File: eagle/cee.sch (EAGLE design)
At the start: 46 parts, among them IC1 IC1, J1 SOLDERJUMPERNC2

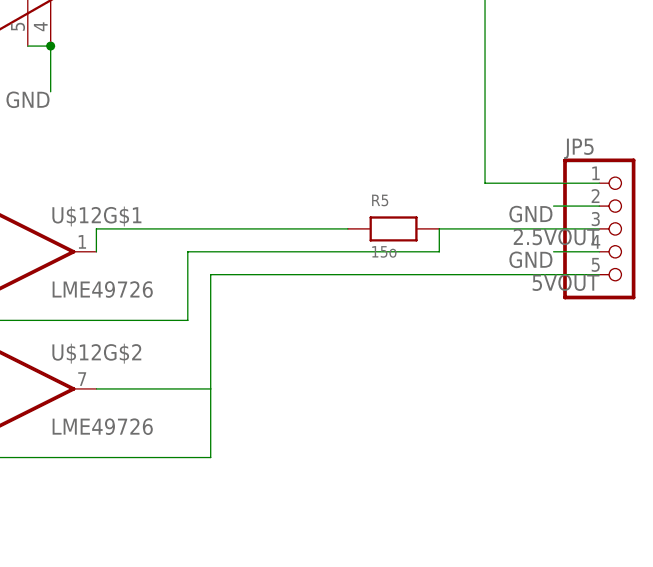
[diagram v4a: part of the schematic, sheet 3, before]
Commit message: pulldown resistor, chanB as input, moved capacitors, updated sc70, cleaned routing
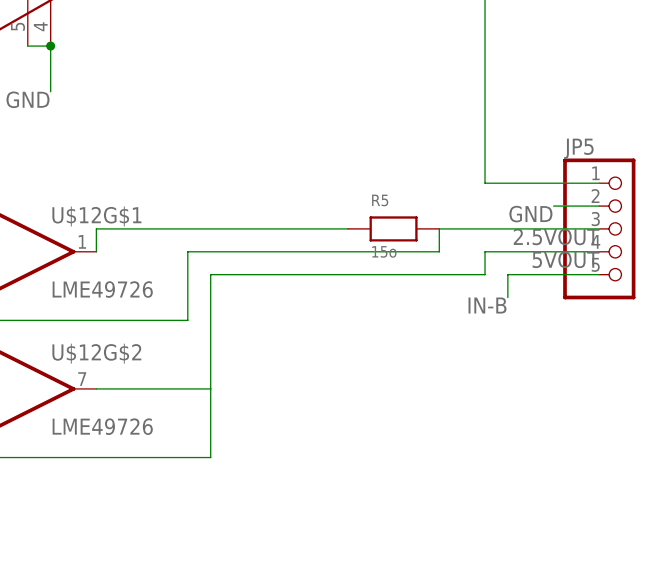
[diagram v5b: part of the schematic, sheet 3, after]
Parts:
- added R7: (no value), nonolith:RESISTOR0603
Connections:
- new net IN-B: JP5.5, R7.2, RN2C.1
- net 5VOUT: now also JP5.4; no longer JP5.5
- net GND: now also R7.1; no longer JP5.4
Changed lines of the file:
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@@
 <part name="C13" library="nonolith" deviceset="CAP_CERAMIC" device="0603" value=".1uF"/>
 <part name="C16" library="nonolith" deviceset="CAP_CERAMIC" device="0603"/>
+<part name="R7" library="nonolith" deviceset="RESISTOR" device="0603"/>
 </parts>
 <sheets>
@@
 <instance part="RN2" gate="B" x="5.08" y="45.72" rot="R90"/>
 <instance part="RN2" gate="C" x="5.08" y="17.78" rot="R90"/>
+<instance part="R7" gate="G$1" x="5.08" y="5.08" rot="R90"/>
 </instances>
 <busses>
@@
 <pinref part="C22" gate="G$1" pin="P$2"/>
 <pinref part="RN1" gate="D" pin="1"/>
+<pinref part="R7" gate="G$1" pin="1"/>
+<wire x1="5.08" y1="0" x2="15.24" y2="0" width="0" layer="91"/>
 </segment>
 <segment>
@@
 <label x="35.56" y="58.42" size="1.778" layer="95"/>
 <pinref part="OPA-C" gate="G$1" pin="V+"/>
+</segment>
+</net>
+<net name="IN-B" class="0">
+<segment>
+<pinref part="RN2" gate="C" pin="1"/>
+<wire x1="5.08" y1="12.7" x2="5.08" y2="10.16" width="0" layer="91"/>
+<label x="5.08" y="10.16" size="1.778" layer="95"/>
+<pinref part="R7" gate="G$1" pin="2"/>
 </segment>
 </net>
@@
 </segment>
 <segment>
-<wire x1="198.12" y1="58.42" x2="193.04" y2="58.42" width="0" layer="91"/>
-<label x="193.04" y="58.42" size="1.778" layer="95" rot="R180"/>
-<pinref part="JP5" gate="A" pin="4"/>
-</segment>
-<segment>
 <pinref part="CS-A" gate="G$1" pin="GND"/>
 <label x="15.24" y="63.5" size="1.778" layer="95" rot="R180"/>
@@
 <net name="5VOUT" class="0">
 <segment>
-<pinref part="JP5" gate="A" pin="5"/>
-<wire x1="198.12" y1="55.88" x2="154.94" y2="55.88" width="0" layer="91"/>
 <wire x1="154.94" y1="55.88" x2="154.94" y2="43.18" width="0" layer="91"/>
 <pinref part="U$12" gate="G$2" pin="OUT"/>
@@
 <wire x1="121.92" y1="35.56" x2="154.94" y2="35.56" width="0" layer="91"/>
 <wire x1="154.94" y1="35.56" x2="154.94" y2="43.18" width="0" layer="91"/>
-<label x="198.12" y="55.88" size="1.778" layer="95" rot="R180"/>
+<label x="198.12" y="58.42" size="1.778" layer="95" rot="R180"/>
+<wire x1="154.94" y1="55.88" x2="185.42" y2="55.88" width="0" layer="91"/>
+<wire x1="185.42" y1="55.88" x2="185.42" y2="58.42" width="0" layer="91"/>
+<pinref part="JP5" gate="A" pin="4"/>
+<wire x1="185.42" y1="58.42" x2="198.12" y2="58.42" width="0" layer="91"/>
 </segment>
 </net>
@@
 </segment>
 </net>
+<net name="IN-B" class="0">
+<segment>
+<pinref part="JP5" gate="A" pin="5"/>
+<wire x1="198.12" y1="55.88" x2="187.96" y2="55.88" width="0" layer="91"/>
+<wire x1="187.96" y1="55.88" x2="187.96" y2="53.34" width="0" layer="91"/>
+<label x="187.96" y="53.34" size="1.778" layer="95" rot="R180"/>
+</segment>
+</net>

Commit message: route tflag
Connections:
- new net TFLAG-P: IC1.PB1/ADC9, R4.2
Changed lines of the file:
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@@
+</segment>
+</net>
+<net name="TFLAG-P" class="0">
+<segment>
+<pinref part="R4" gate="G$1" pin="2"/>
+<wire x1="45.72" y1="96.52" x2="50.8" y2="96.52" width="0" layer="91"/>
+<label x="50.8" y="96.52" size="1.778" layer="95"/>
+</segment>
+<segment>
+<pinref part="IC1" gate="G$1" pin="PB1/ADC9"/>
+<wire x1="96.52" y1="33.02" x2="101.6" y2="33.02" width="0" layer="91"/>
+<label x="101.6" y="33.02" size="1.778" layer="95"/>
 </segment>
 </net>

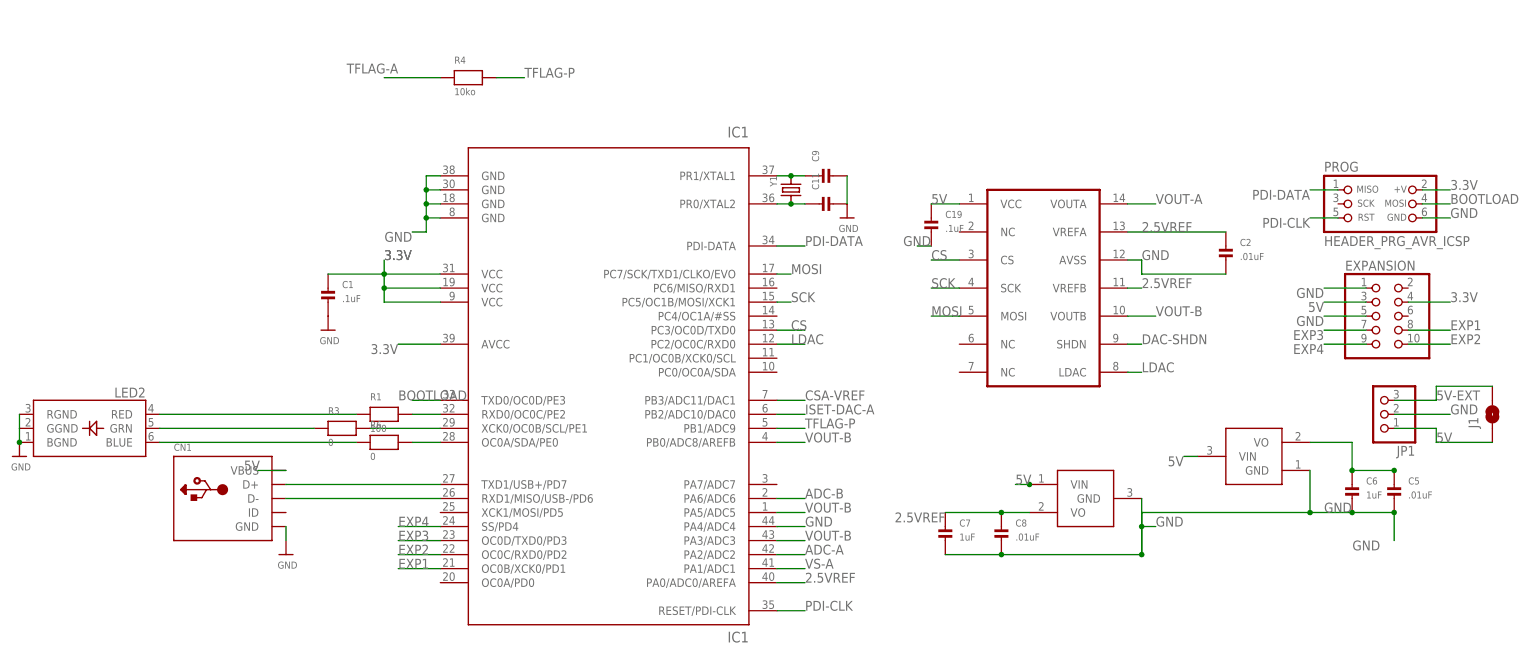
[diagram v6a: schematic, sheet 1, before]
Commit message: Clean up, route digital lines
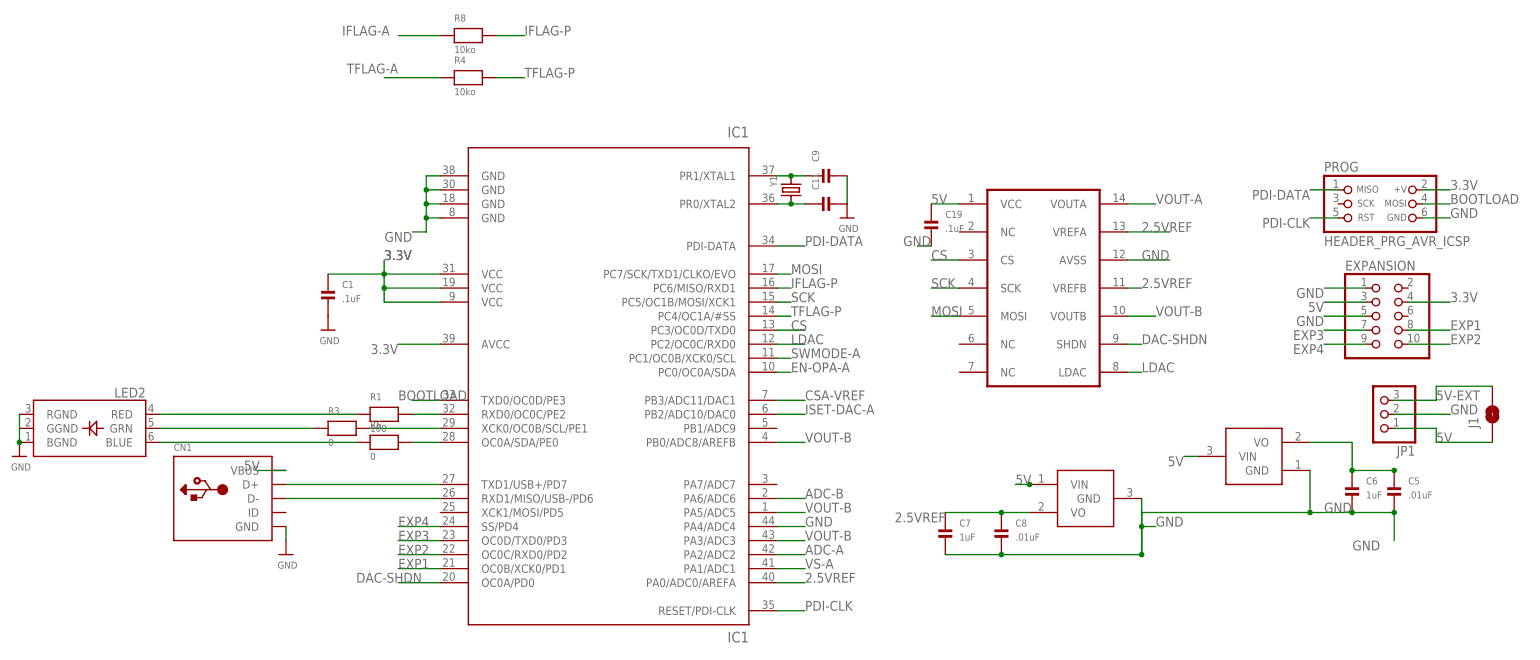
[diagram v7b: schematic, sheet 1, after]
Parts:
- removed C2: .01uF, nonolith:CAP_CERAMIC0603
- added C17: .1uF, nonolith:CAP_CERAMIC0603
- added R8: 10ko, nonolith:RESISTOR0603
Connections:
- new net IFLAG-A: OPA-A.IFLAG, R8.1
- new net IFLAG-P: IC1.PC6/MISO/RXD1, R8.2
- net 2.5VREF: no longer C2.P$1
- net 5V: now also C17.P$2; no longer C13.P$1, C3.P$1, U$12G$2.+IN, U$12G$3.V+
- net 5V-EXT: now also C13.P$1, C3.P$1, U$12G$2.+IN, U$12G$3.V+
- net DAC-SHDN: now also IC1.OC0A/PD0
- net EN-OPA-A: now also IC1.PC0/OC0A/SDA
- net GND: now also C17.P$1; no longer C2.P$2
- net SWMODE-A: now also IC1.PC1/OC0B/XCK0/SCL
- net TFLAG-P: now also IC1.PC4/OC1A/#SS; no longer IC1.PB1/ADC9
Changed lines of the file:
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@@
 <?xml version="1.0" encoding="utf-8"?>
 <!DOCTYPE eagle SYSTEM "eagle.dtd">
-<eagle version="6.3">
+<eagle version="6.1">
 <drawing>
 <settings>
@@
 <part name="C8" library="nonolith" deviceset="CAP_CERAMIC" device="0603" value=".01uF"/>
 <part name="2.5REF" library="nonolith" deviceset="VREF" device="" value=""/>
-<part name="C2" library="nonolith" deviceset="CAP_CERAMIC" device="0603" value=".01uF"/>
 <part name="J1" library="SparkFun" deviceset="SOLDERJUMPER" device="NC2"/>
 <part name="3.3VREG" library="nonolith" deviceset="VREG" device="" value=""/>
@@
 <part name="C16" library="nonolith" deviceset="CAP_CERAMIC" device="0603"/>
 <part name="R7" library="nonolith" deviceset="RESISTOR" device="0603"/>
+<part name="C17" library="nonolith" deviceset="CAP_CERAMIC" device="0603" value=".1uF"/>
+<part name="R8" library="nonolith" deviceset="RESISTOR" device="0603" value="10ko"/>
 </parts>
 <sheets>
@@
 <instance part="C8" gate="G$1" x="137.16" y="12.7"/>
 <instance part="2.5REF" gate="G$1" x="152.4" y="20.32" rot="R180"/>
-<instance part="C2" gate="G$1" x="177.8" y="63.5"/>
 <instance part="J1" gate="1" x="226.06" y="35.56" smashed="yes" rot="R90">
 <attribute name="NAME" x="223.52" y="33.02" size="1.778" layer="95" rot="R90"/>
@@
 <instance part="R6" gate="G$1" x="25.4" y="30.48"/>
 <instance part="U$7" gate="G$1" x="-40.64" y="27.94"/>
+<instance part="R8" gate="G$1" x="40.64" y="104.14"/>
 </instances>
 <busses>
@@
 </segment>
 <segment>
-<wire x1="160.02" y1="63.5" x2="162.56" y2="63.5" width="0" layer="91"/>
-<wire x1="162.56" y1="63.5" x2="162.56" y2="60.96" width="0" layer="91"/>
-<wire x1="162.56" y1="60.96" x2="177.8" y2="60.96" width="0" layer="91"/>
+<wire x1="160.02" y1="63.5" x2="167.64" y2="63.5" width="0" layer="91"/>
 <label x="162.56" y="63.5" size="1.778" layer="95"/>
 <pinref part="DAC" gate="G$1" pin="AVSS"/>
-<pinref part="C2" gate="G$1" pin="P$2"/>
 </segment>
 <segment>
@@
 </segment>
 <segment>
-<wire x1="160.02" y1="68.58" x2="177.8" y2="68.58" width="0" layer="91"/>
+<wire x1="160.02" y1="68.58" x2="167.64" y2="68.58" width="0" layer="91"/>
 <label x="162.56" y="68.58" size="1.778" layer="95"/>
 <pinref part="DAC" gate="G$1" pin="VREFA"/>
-<pinref part="C2" gate="G$1" pin="P$1"/>
 </segment>
 <segment>
@@
 <pinref part="DAC" gate="G$1" pin="SHDN"/>
 </segment>
+<segment>
+<pinref part="IC1" gate="G$1" pin="OC0A/PD0"/>
+<wire x1="35.56" y1="5.08" x2="27.94" y2="5.08" width="0.1524" layer="91"/>
+<label x="20.32" y="5.08" size="1.778" layer="95"/>
+</segment>
 </net>
 <net name="LDAC" class="0">
@@
 </segment>
 <segment>
-<pinref part="IC1" gate="G$1" pin="PB1/ADC9"/>
-<wire x1="96.52" y1="33.02" x2="101.6" y2="33.02" width="0" layer="91"/>
-<label x="101.6" y="33.02" size="1.778" layer="95"/>
+<pinref part="IC1" gate="G$1" pin="PC4/OC1A/#SS"/>
+<wire x1="96.52" y1="53.34" x2="99.06" y2="53.34" width="0.1524" layer="91"/>
+<label x="99.06" y="53.34" size="1.778" layer="95"/>
+</segment>
+</net>
+<net name="EN-OPA-A" class="0">
+<segment>
+<pinref part="IC1" gate="G$1" pin="PC0/OC0A/SDA"/>
+<wire x1="96.52" y1="43.18" x2="99.06" y2="43.18" width="0.1524" layer="91"/>
+<label x="99.06" y="43.18" size="1.778" layer="95"/>
+</segment>
+</net>
+<net name="SWMODE-A" class="0">
+<segment>
+<pinref part="IC1" gate="G$1" pin="PC1/OC0B/XCK0/SCL"/>
+<wire x1="96.52" y1="45.72" x2="99.06" y2="45.72" width="0.1524" layer="91"/>
+<label x="99.06" y="45.72" size="1.778" layer="95"/>
+</segment>
+</net>
+<net name="IFLAG-A" class="0">
+<segment>
+<pinref part="R8" gate="G$1" pin="1"/>
+<wire x1="35.56" y1="104.14" x2="27.94" y2="104.14" width="0.1524" layer="91"/>
+<label x="17.78" y="104.14" size="1.778" layer="95"/>
+</segment>
+</net>
+<net name="IFLAG-P" class="0">
+<segment>
+<pinref part="R8" gate="G$1" pin="2"/>
+<wire x1="45.72" y1="104.14" x2="50.8" y2="104.14" width="0.1524" layer="91"/>
+<label x="50.8" y="104.14" size="1.778" layer="95"/>
+</segment>
+<segment>
+<pinref part="IC1" gate="G$1" pin="PC6/MISO/RXD1"/>
+<wire x1="96.52" y1="58.42" x2="99.06" y2="58.42" width="0.1524" layer="91"/>
+<label x="99.06" y="58.42" size="1.778" layer="95"/>
 </segment>
 </net>
@@
 <instance part="C13" gate="G$1" x="78.74" y="35.56"/>
 <instance part="C16" gate="G$1" x="116.84" y="55.88"/>
+<instance part="C17" gate="G$1" x="43.18" y="93.98" rot="R180"/>
 </instances>
 <busses>
@@
 <label x="33.02" y="99.06" size="1.778" layer="95" rot="R180"/>
 <pinref part="C4" gate="G$1" pin="P$2"/>
+<pinref part="C17" gate="G$1" pin="P$2"/>
+<wire x1="33.02" y1="96.52" x2="43.18" y2="96.52" width="0.1524" layer="91"/>
 </segment>
 <segment>
@@
 <wire x1="22.86" y1="58.42" x2="17.78" y2="58.42" width="0" layer="91"/>
 <label x="17.78" y="58.42" size="1.778" layer="95" rot="R180"/>
-</segment>
-<segment>
-<pinref part="U$12" gate="G$2" pin="+IN"/>
-<pinref part="U$12" gate="G$3" pin="V+"/>
-<wire x1="127" y1="45.72" x2="106.68" y2="45.72" width="0" layer="91"/>
-<pinref part="C13" gate="G$1" pin="P$1"/>
-<pinref part="C3" gate="G$1" pin="P$1"/>
-<wire x1="78.74" y1="40.64" x2="91.44" y2="40.64" width="0" layer="91"/>
-<wire x1="91.44" y1="40.64" x2="104.14" y2="40.64" width="0" layer="91"/>
-<wire x1="104.14" y1="40.64" x2="104.14" y2="45.72" width="0" layer="91"/>
-<wire x1="104.14" y1="45.72" x2="106.68" y2="45.72" width="0" layer="91"/>
-<label x="78.74" y="40.64" size="1.778" layer="95" rot="R180"/>
 </segment>
 </net>
@@
 <wire x1="33.02" y1="88.9" x2="33.02" y2="86.36" width="0" layer="91"/>
 <label x="33.02" y="86.36" size="1.778" layer="95"/>
+<pinref part="C17" gate="G$1" pin="P$1"/>
+<wire x1="43.18" y1="88.9" x2="33.02" y2="88.9" width="0.1524" layer="91"/>
 </segment>
 <segment>
@@
 <pinref part="C14" gate="G$1" pin="P$1"/>
 <pinref part="C15" gate="G$1" pin="P$1"/>
+</segment>
+<segment>
+<pinref part="C13" gate="G$1" pin="P$1"/>
+<pinref part="C3" gate="G$1" pin="P$1"/>
+<wire x1="78.74" y1="40.64" x2="91.44" y2="40.64" width="0.1524" layer="91"/>
+<wire x1="91.44" y1="40.64" x2="104.14" y2="40.64" width="0.1524" layer="91"/>
+<wire x1="104.14" y1="40.64" x2="104.14" y2="45.72" width="0.1524" layer="91"/>
+<pinref part="U$12" gate="G$3" pin="V+"/>
+<wire x1="104.14" y1="45.72" x2="106.68" y2="45.72" width="0.1524" layer="91"/>
+<pinref part="U$12" gate="G$2" pin="+IN"/>
+<wire x1="106.68" y1="45.72" x2="127" y2="45.72" width="0.1524" layer="91"/>
+<label x="78.74" y="40.64" size="1.778" layer="95"/>
 </segment>
 </net>
@@
 </segment>
 </net>
+<net name="IFLAG-A" class="0">
+<segment>
+<pinref part="OPA-A" gate="G$1" pin="IFLAG"/>
+<wire x1="114.3" y1="91.44" x2="109.22" y2="91.44" width="0.1524" layer="91"/>
+<label x="109.22" y="91.44" size="1.778" layer="95" rot="R180"/>
+</segment>
+</net>

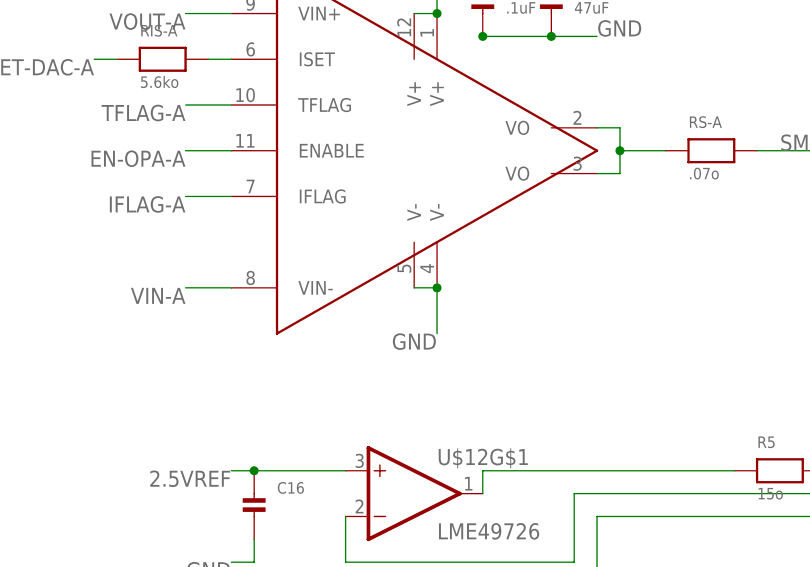
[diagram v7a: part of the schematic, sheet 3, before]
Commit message: Update library (SC70 and QFN)
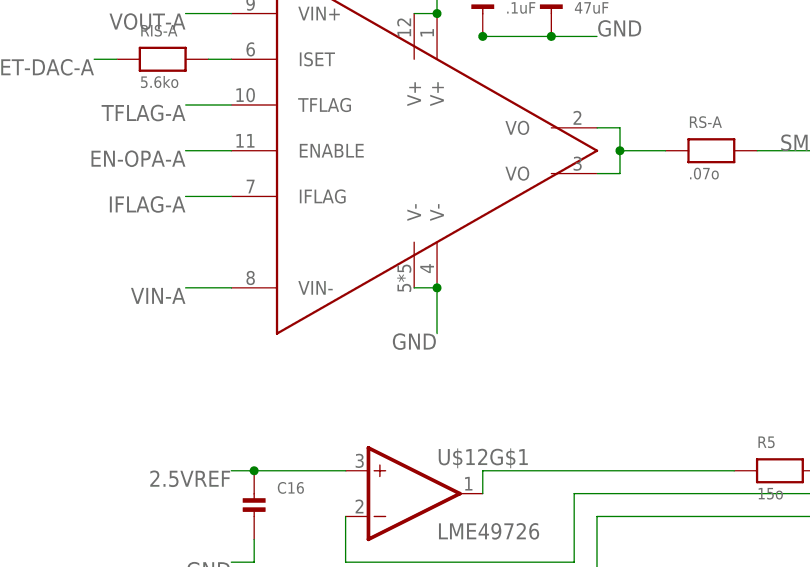
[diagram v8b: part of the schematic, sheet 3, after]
